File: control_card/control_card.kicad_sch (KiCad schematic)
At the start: 46 parts, among them IC1 TLSR8253F512ET48, J1 Conn_02x04_Counter_Clockwise, J2 Conn_01x01_Pin, J3 Conn_01x01_Pin, J4 Conn_01x01_Pin, J5 Conn_01x01_Pin, U1 Wifi, Y1 Crystal_GND24_Small

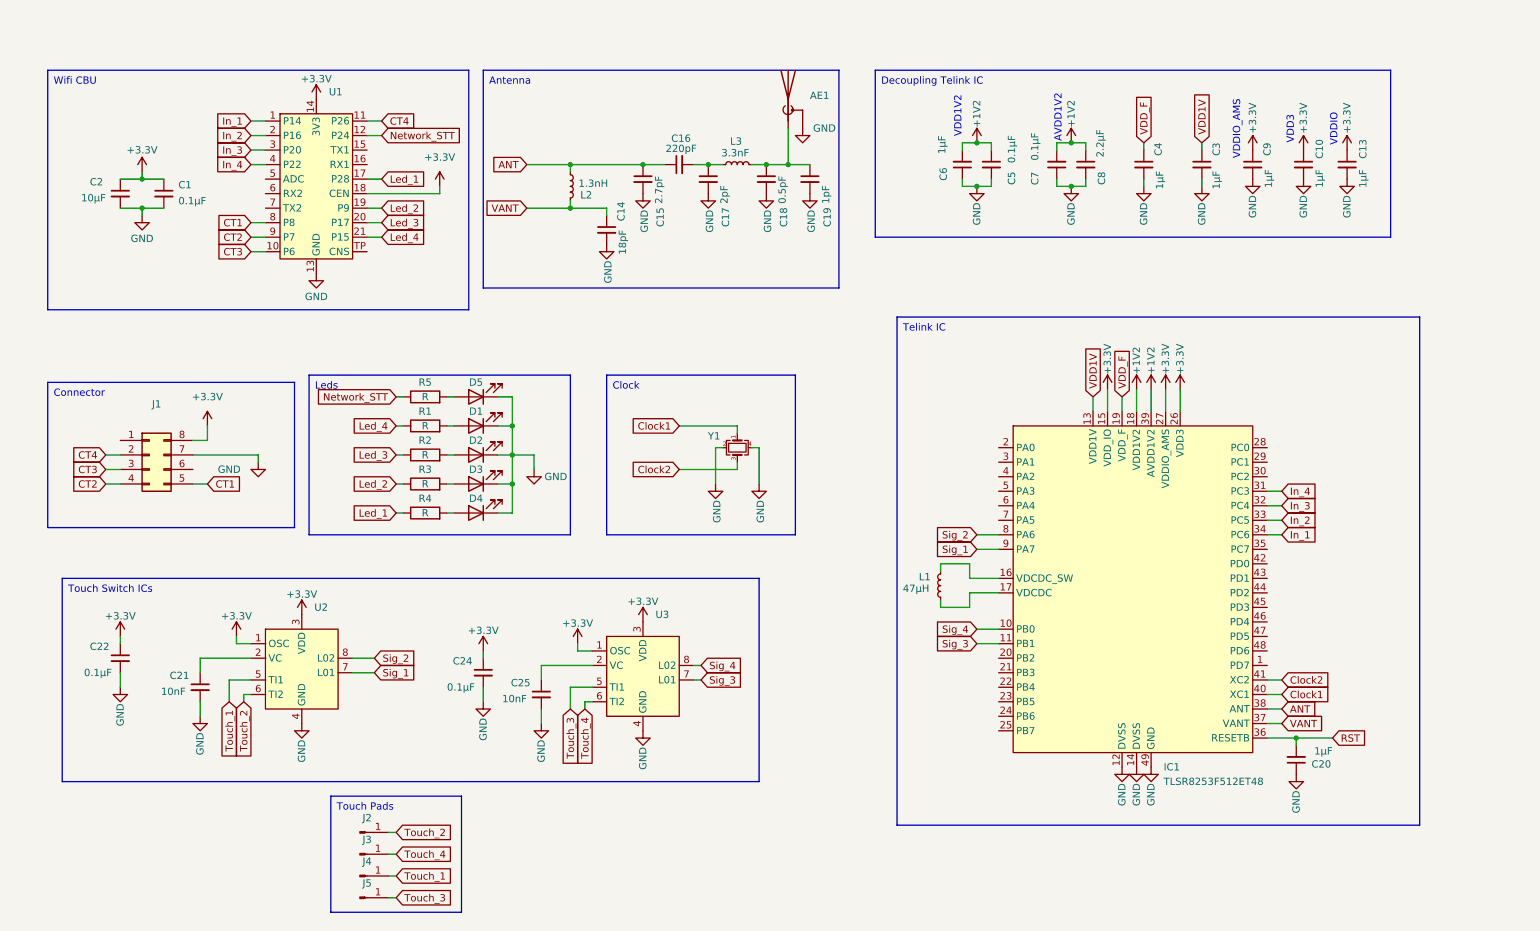
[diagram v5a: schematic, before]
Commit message: PCB (control_card) : Test point added
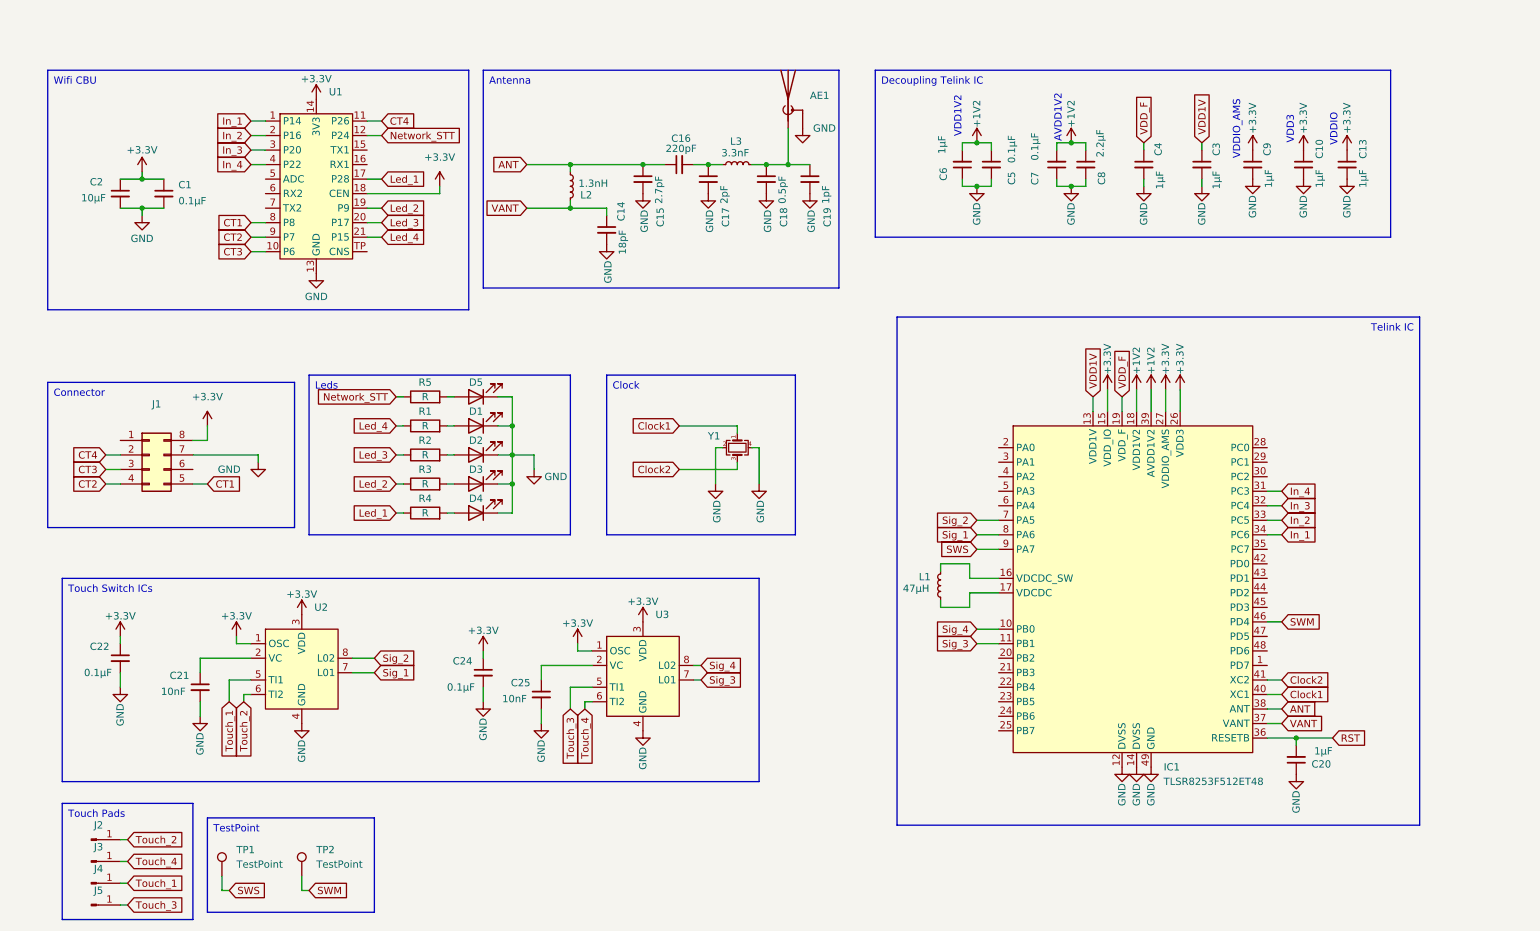
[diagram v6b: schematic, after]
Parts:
- added TP1, TP2: TestPoint, TestPoint:TestPoint_Pad_D1.0mm, symbol Connector:TestPoint
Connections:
- net Sig_1: now also IC1.8 (PA6); no longer IC1.9 (PA7)
- net Sig_2: now also IC1.7 (PA5); no longer IC1.8 (PA6)
- net SWM: now reaches IC1.46 (PD4)
- net SWM: now also TP2.1
- new net SWS: IC1.9 (PA7), TP1.1
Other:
- moved on the sheet: J2, J3, J4, J5
